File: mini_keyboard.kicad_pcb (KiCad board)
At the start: 2 copper layers, 232.4 x 175.3 mm, 47 parts, among them J1 Conn_01x05_Male, SW1 SW_DIP_x01, SW10 SW_DIP_x01, SW11 SW_DIP_x01, SW12 SW_DIP_x01, SW13 SW_DIP_x01, SW14 SW_DIP_x01, SW15 SW_DIP_x01, SW16 SW_DIP_x01, SW17 SW_DIP_x01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

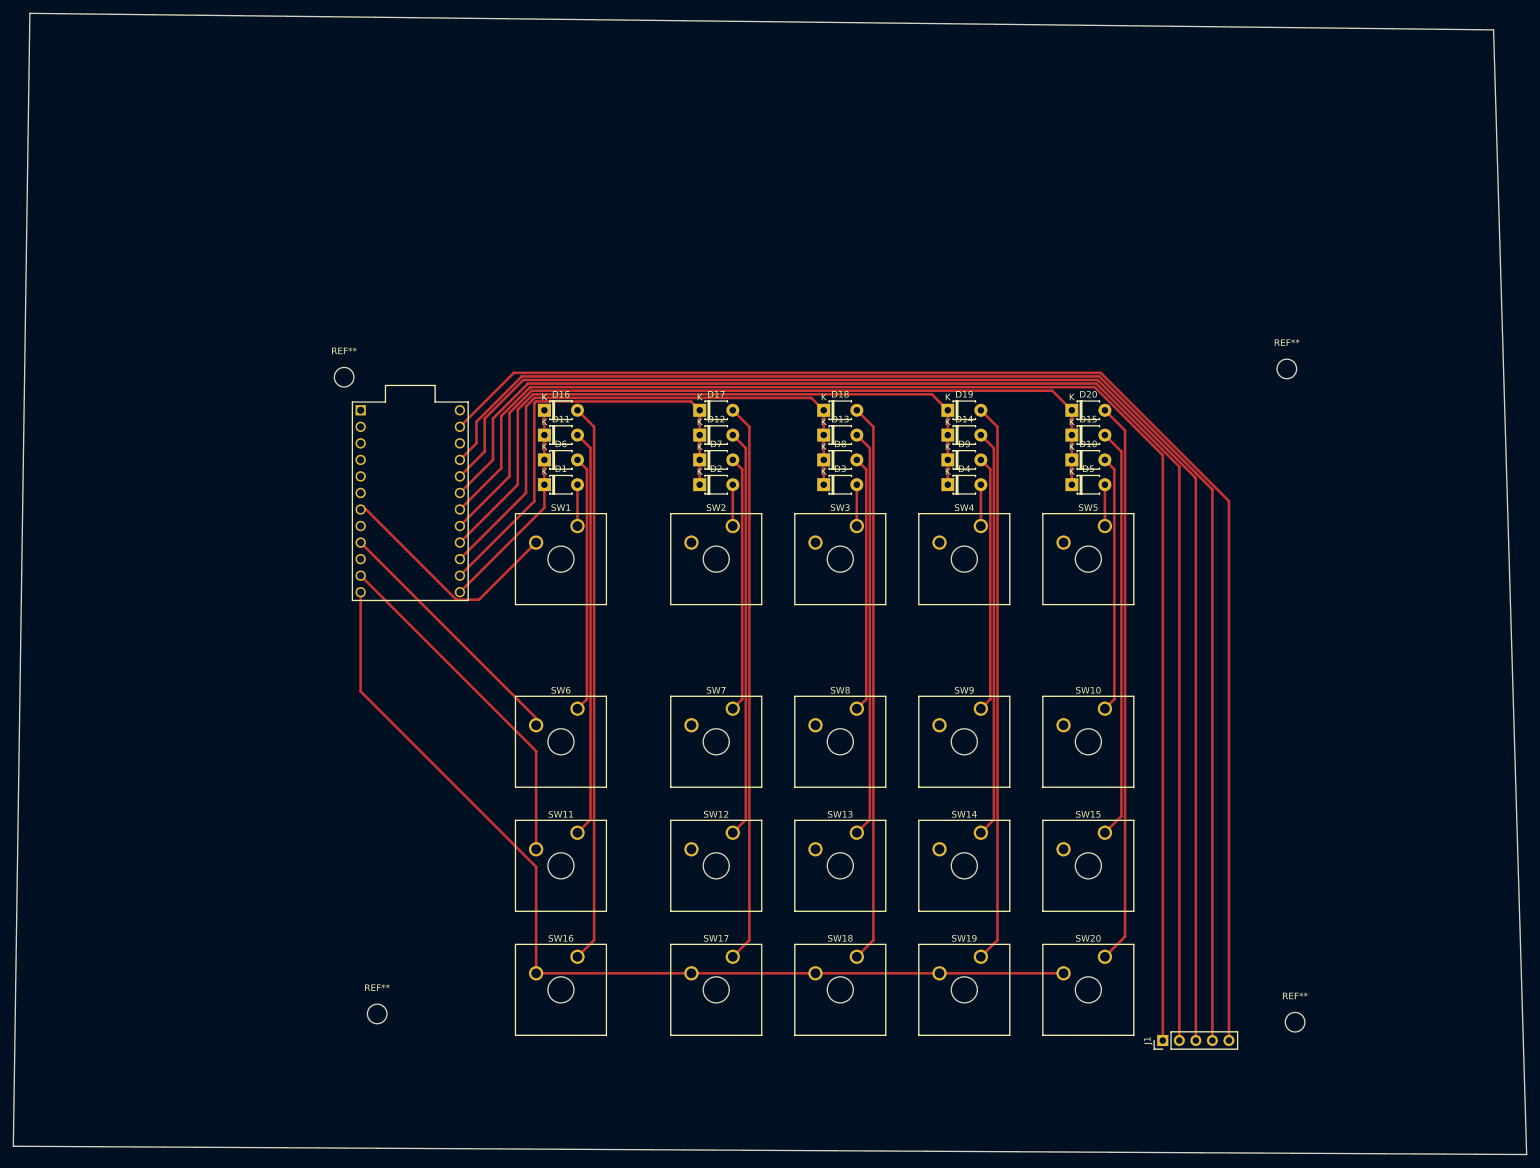
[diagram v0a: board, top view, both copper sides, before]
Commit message: Made edge smaller
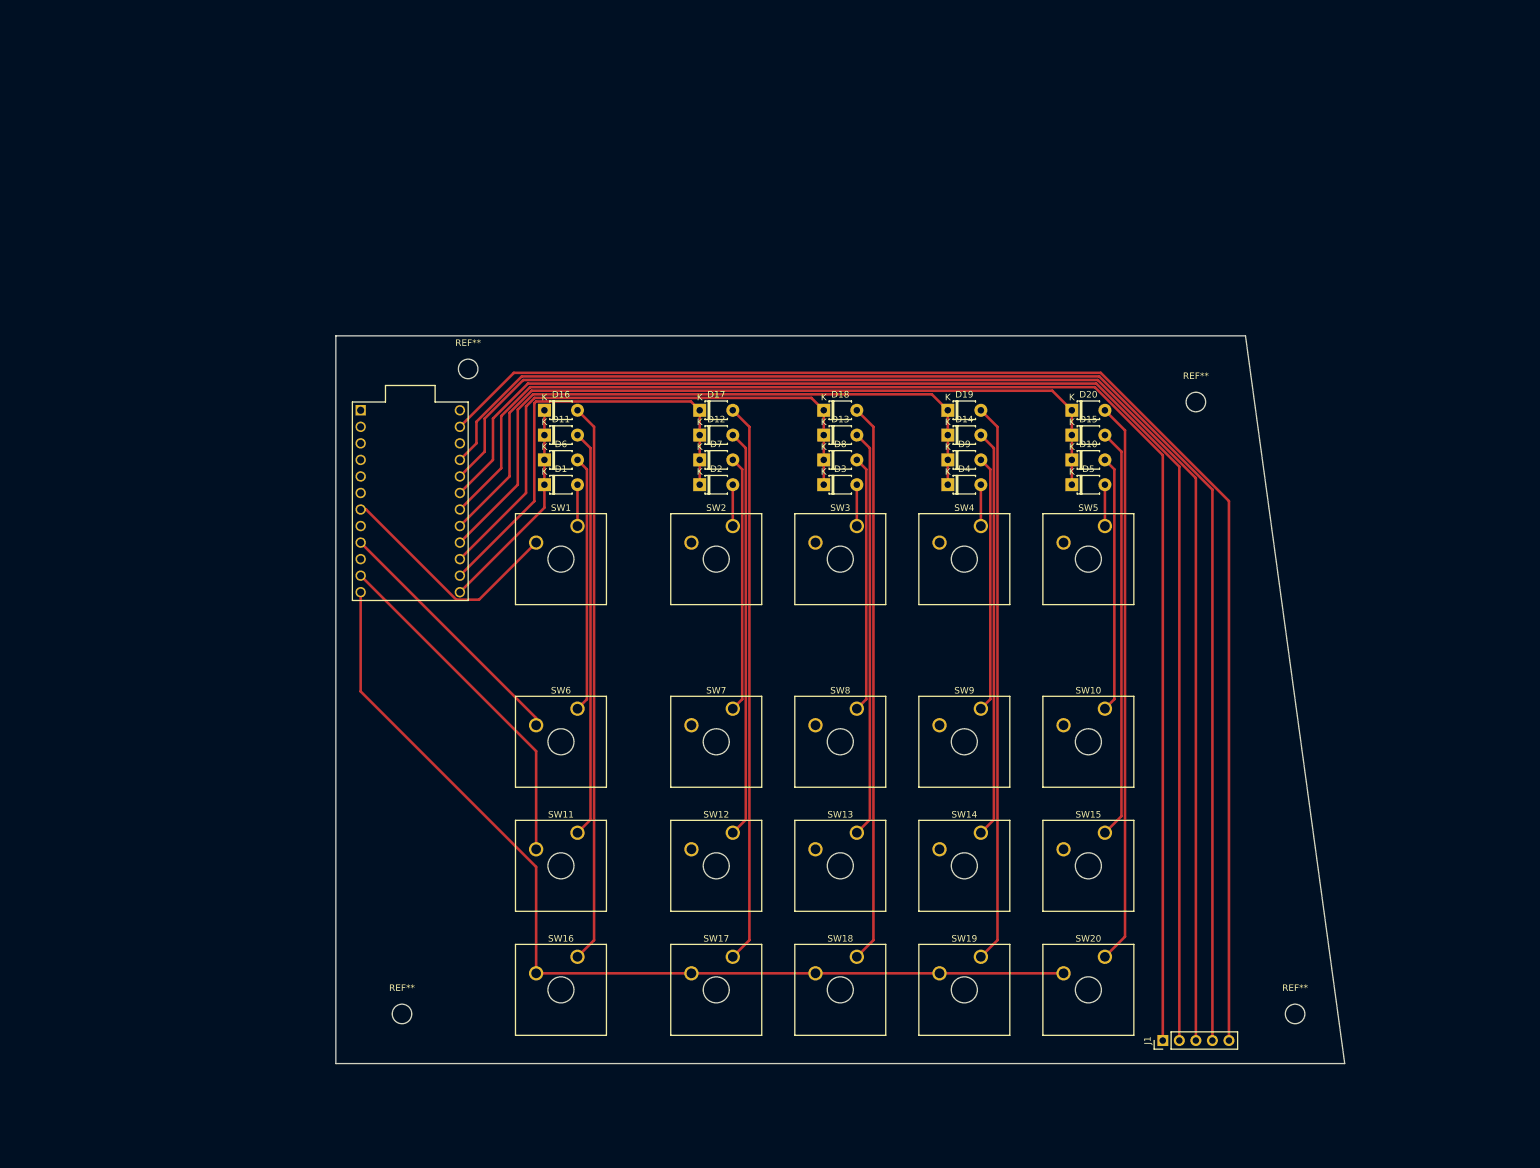
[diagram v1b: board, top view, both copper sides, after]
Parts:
- moved REF** 19.1 mm to (81.3, 35.6)
- moved REF** 14.9 mm to (193.0, 40.6)
- moved REF** 3.81 mm to (71.1, 134.6)
- moved REF** 1.27 mm to (208.3, 134.6)
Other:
- board size 232.4 x 175.3 mm -> 154.9 x 111.8 mm

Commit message: made some design rules changes
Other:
- net class Power removed

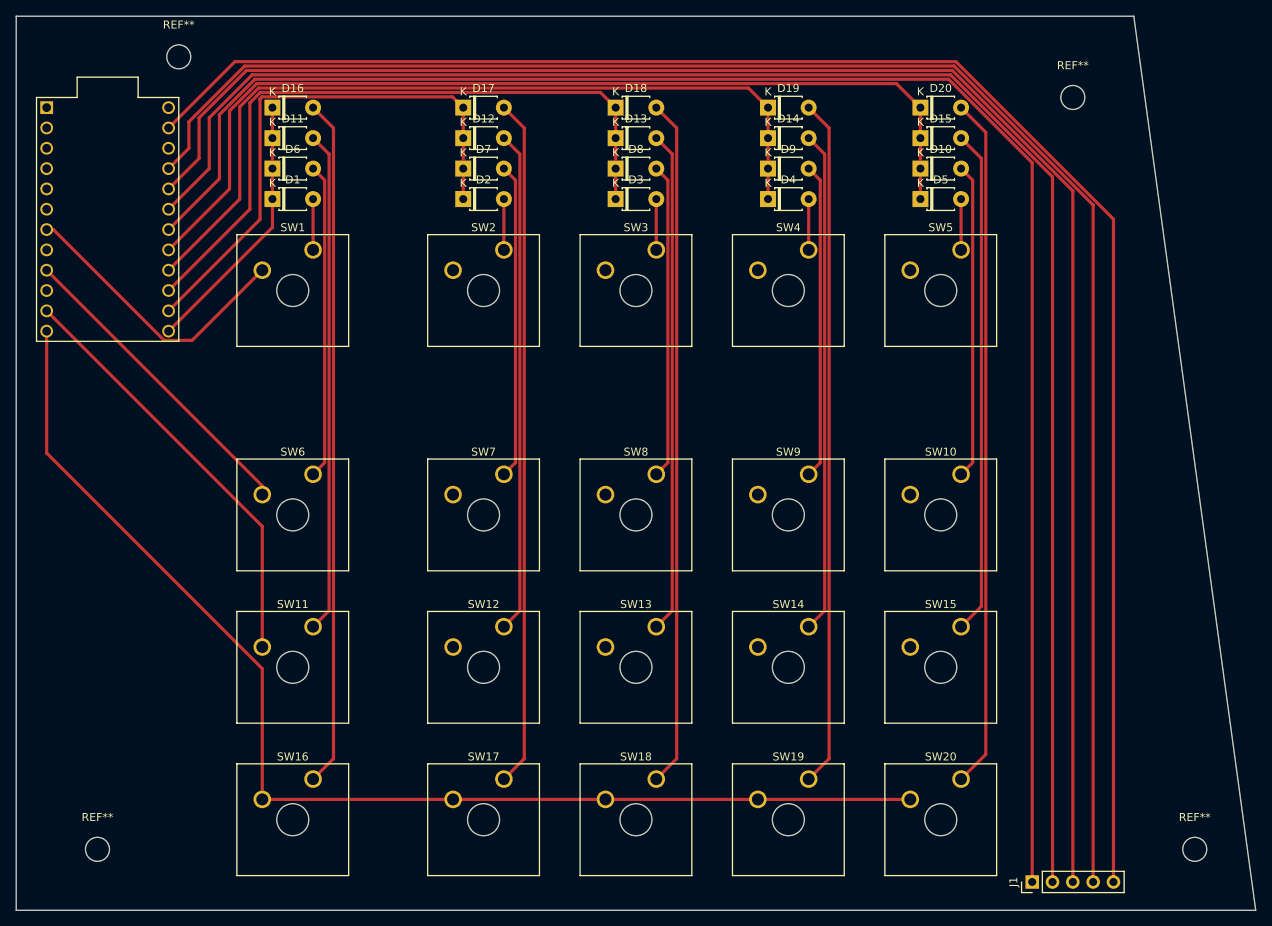
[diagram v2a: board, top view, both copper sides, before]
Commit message: Update netlist. Wider left side
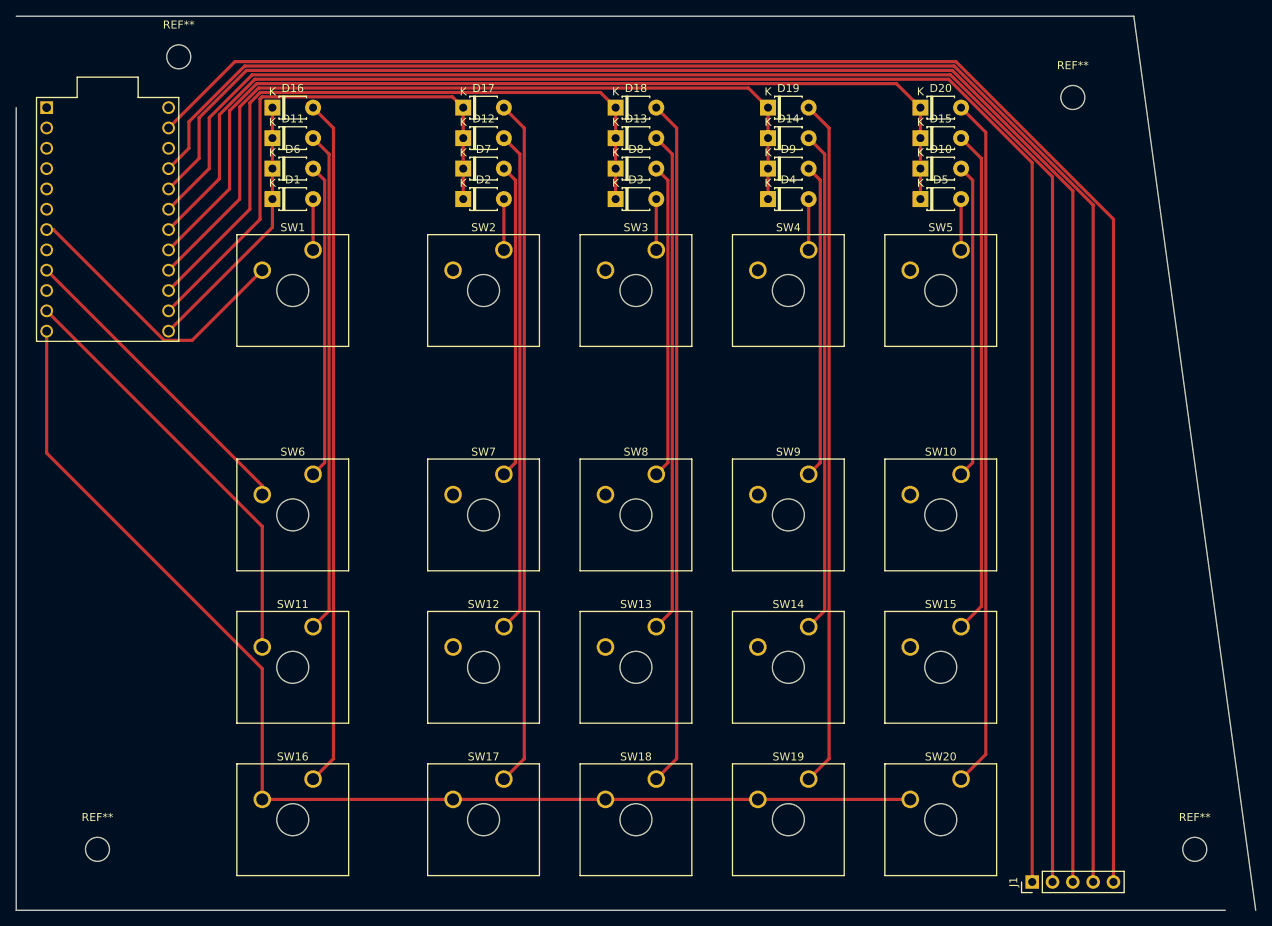
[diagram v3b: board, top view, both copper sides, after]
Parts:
- SW1, SW11, SW16, SW6: footprint Button_Switch_Keyboard:SW_Cherry_MX_1.00u_Plate -> Button_Switch_Keyboard:SW_Cherry_MX_1.50u_Plate
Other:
- outline, holes or cut-outs redrawn

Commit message: clearance 0.3 Lines pressed at top
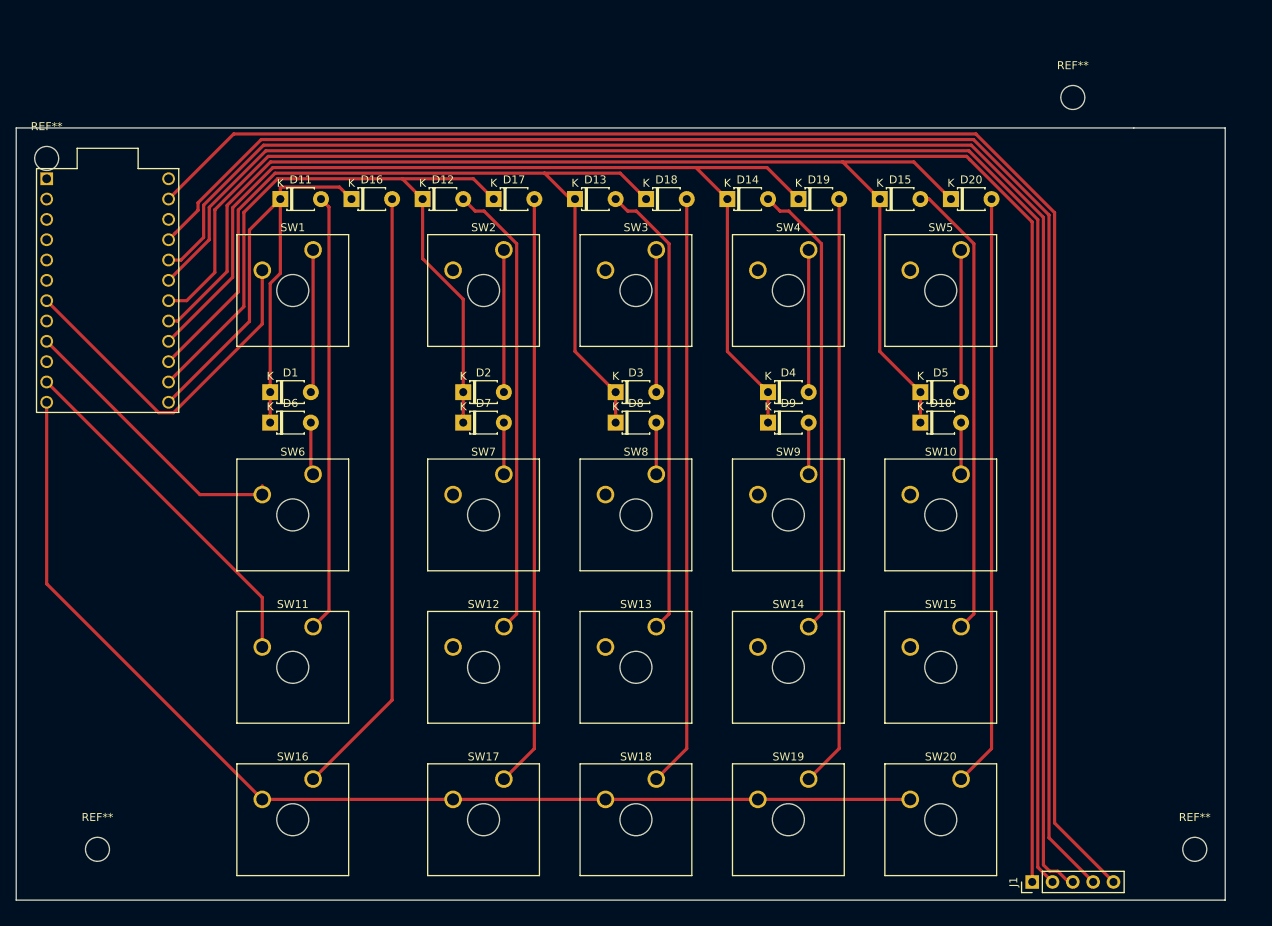
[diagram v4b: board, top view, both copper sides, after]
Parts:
- moved D6 31.8 mm to (92.7, 81.3)
- moved D10 31.8 mm to (174.0, 81.3)
- moved D7 31.8 mm to (116.8, 81.3)
- moved D8 31.8 mm to (135.9, 81.3)
- moved D9 31.8 mm to (154.9, 81.3)
- moved D1 24.1 mm to (92.7, 77.5)
- moved D2 24.1 mm to (116.8, 77.5)
- moved D3 24.1 mm to (135.9, 77.5)
- moved D4 24.1 mm to (154.9, 77.5)
- moved D5 24.1 mm to (174.0, 77.5)
- moved REF** 20.8 mm to (64.8, 48.3)
- moved D16 15.1 mm to (102.9, 53.3)
- moved D17 12.0 mm to (120.7, 53.3)
- moved D18 12.0 mm to (139.7, 53.3)
- moved D19 12.0 mm to (158.8, 53.3)
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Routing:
- net /in1: track 33.3 -> 71.3 mm
- net Net-(D8-Pad2): track 39.4 -> 6.46 mm
- net Net-(D10-Pad2): track 39.4 -> 6.46 mm
- net Net-(D7-Pad2): track 39.4 -> 6.46 mm
- net Net-(D9-Pad2): track 39.4 -> 6.46 mm
- net Net-(D6-Pad2): track 39.4 -> 6.58 mm
- net /in5: track 121.0 -> 149.4 mm
- net /in4: track 103.6 -> 130.7 mm
- net /in3: track 86.1 -> 112.0 mm
- net /in2: track 68.7 -> 93.0 mm
- net Net-(D20-Pad2): track 86.5 -> 74.1 mm
- net Net-(D18-Pad2): track 86.0 -> 74.1 mm
- net Net-(D17-Pad2): track 86.0 -> 74.1 mm
- net Net-(D19-Pad2): track 86.0 -> 74.1 mm
- net Net-(D1-Pad2): track 6.35 -> 17.9 mm
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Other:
- board size 154.9 x 111.8 mm -> 151.1 x 96.5 mm
- net class Default: clearance 0.15 -> 0.3
- rule trace_clearance: 0.15 -> 0.3

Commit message: lines done
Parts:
- moved REF** 14.8 mm to (205.7, 48.3)
- moved U1 2.54 mm to (72.4, 67.3)
- moved REF** 2.54 mm to (205.7, 134.6)
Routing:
- net /in3: track 112.0 -> 114.7 mm
- net /in4: track 130.7 -> 133.2 mm
- net Net-(J1-Pad2): track 204.8 -> 207.4 mm
- net /in1: track 71.3 -> 73.8 mm
- net Net-(J1-Pad4): track 205.3 -> 207.9 mm
- net /out3: track 44.3 -> 41.8 mm
- net /out1: track 44.1 -> 46.6 mm
- net /in2: track 93.0 -> 95.5 mm
- net /out2: track 36.0 -> 33.8 mm
- net /in5: track 149.4 -> 151.3 mm
- net Net-(J1-Pad3): track 206.9 -> 208.5 mm
- net /out4: track 141.8 -> 140.3 mm
- net Net-(J1-Pad5): track 204.9 -> 206.2 mm
- net Net-(J1-Pad1): track 205.9 -> 207.1 mm
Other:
- board size 151.1 x 96.5 mm -> 148.6 x 96.5 mm

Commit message: minor edit
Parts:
- moved REF** 6.84 mm to (64.8, 137.2)
- moved REF** 2.54 mm to (205.7, 137.2)
- moved U1 1.80 mm to (71.1, 68.6)
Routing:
- net /out4: track 140.3 -> 138.5 mm
- net Net-(J1-Pad5): track 206.2 -> 208.0 mm
- net Net-(J1-Pad4): track 207.9 -> 209.7 mm
- net /in5: track 151.3 -> 153.1 mm
- net /in4: track 133.2 -> 135.0 mm
- net Net-(J1-Pad3): track 208.5 -> 210.3 mm
- net /out1: track 46.6 -> 48.4 mm
- net /in2: track 95.5 -> 97.3 mm
- net /in1: track 73.8 -> 75.6 mm
- net Net-(J1-Pad2): track 207.4 -> 209.2 mm
- net Net-(J1-Pad1): track 207.1 -> 208.9 mm
- net /in3: track 114.7 -> 116.5 mm
- net /out2: track 33.8 -> 34.6 mm
- net /out3: track 41.8 -> 42.5 mm
- added copper zone on F.Cu, net (none)

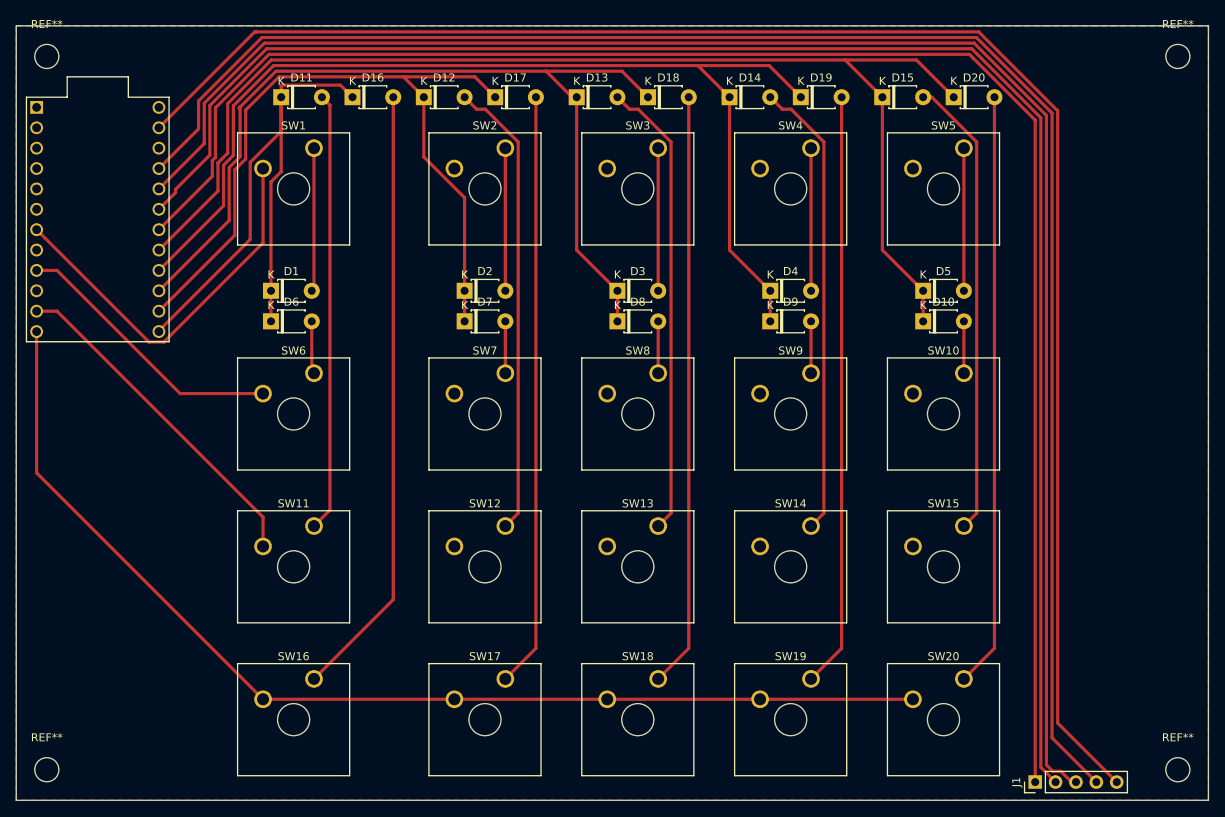
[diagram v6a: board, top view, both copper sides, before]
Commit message: Moved holes a bit
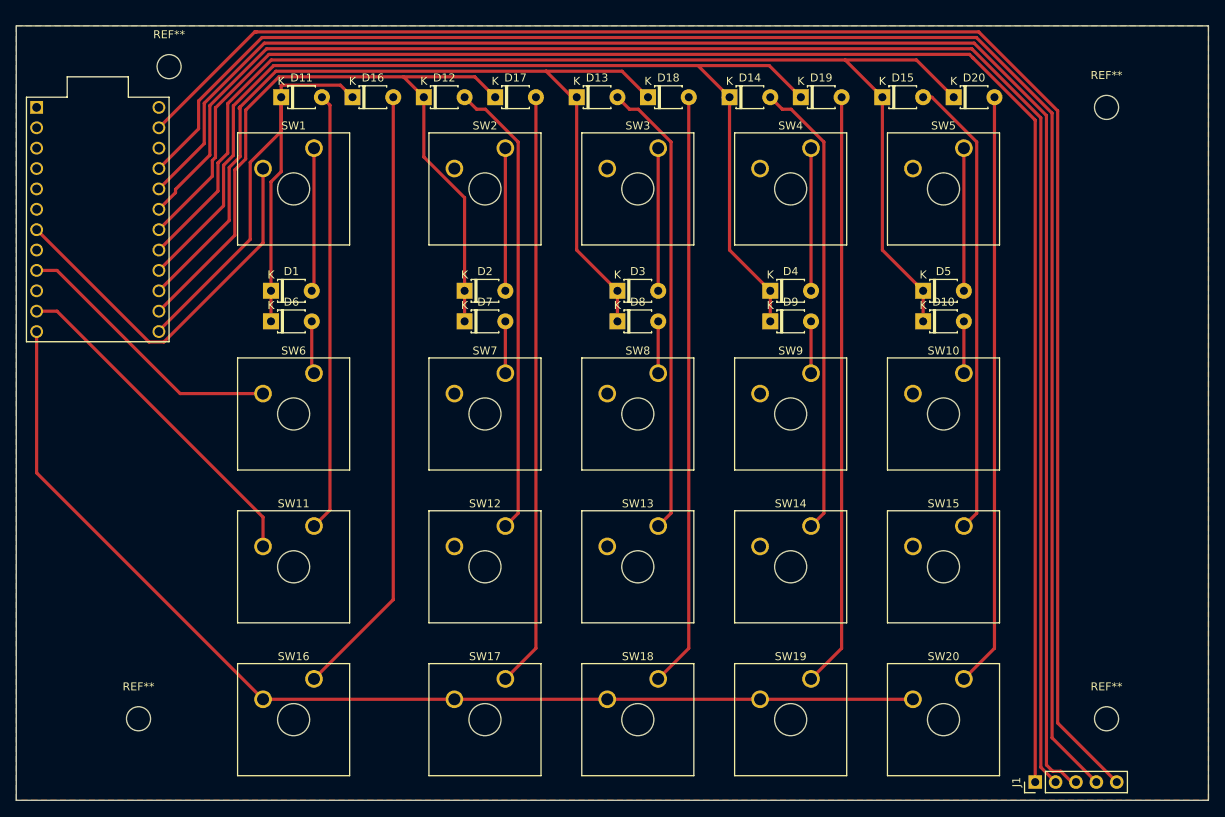
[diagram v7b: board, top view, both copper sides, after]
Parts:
- moved REF** 15.3 mm to (80.0, 49.5)
- moved REF** 13.1 mm to (76.2, 130.8)
- moved REF** 10.9 mm to (196.8, 54.6)
- moved REF** 10.9 mm to (196.8, 130.8)

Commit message: No extra cables
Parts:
- moved ? 29.0 mm to (61.0, 110.5)
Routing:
- net /out1: track 48.4 -> 547.4 mm
- net /out2: track 34.6 -> 392.1 mm
- net /out3: track 42.5 -> 260.5 mm
- net /out4: track 138.5 -> 178.8 mm
